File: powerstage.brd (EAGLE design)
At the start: 42 x 43.5 mm, 42 parts, among them CON1 PINHEAD_1X10-2-FEMALE, CON2 BATTERY_CON-2P-XT30-RA, CON3 PINHEAD_1X10-2-FEMALE, IC5 MCP9700, Q1 BUK9K6R2-40E,115, Q2 BUK9K6R2-40E,115, Q3 BUK9K6R2-40E,115

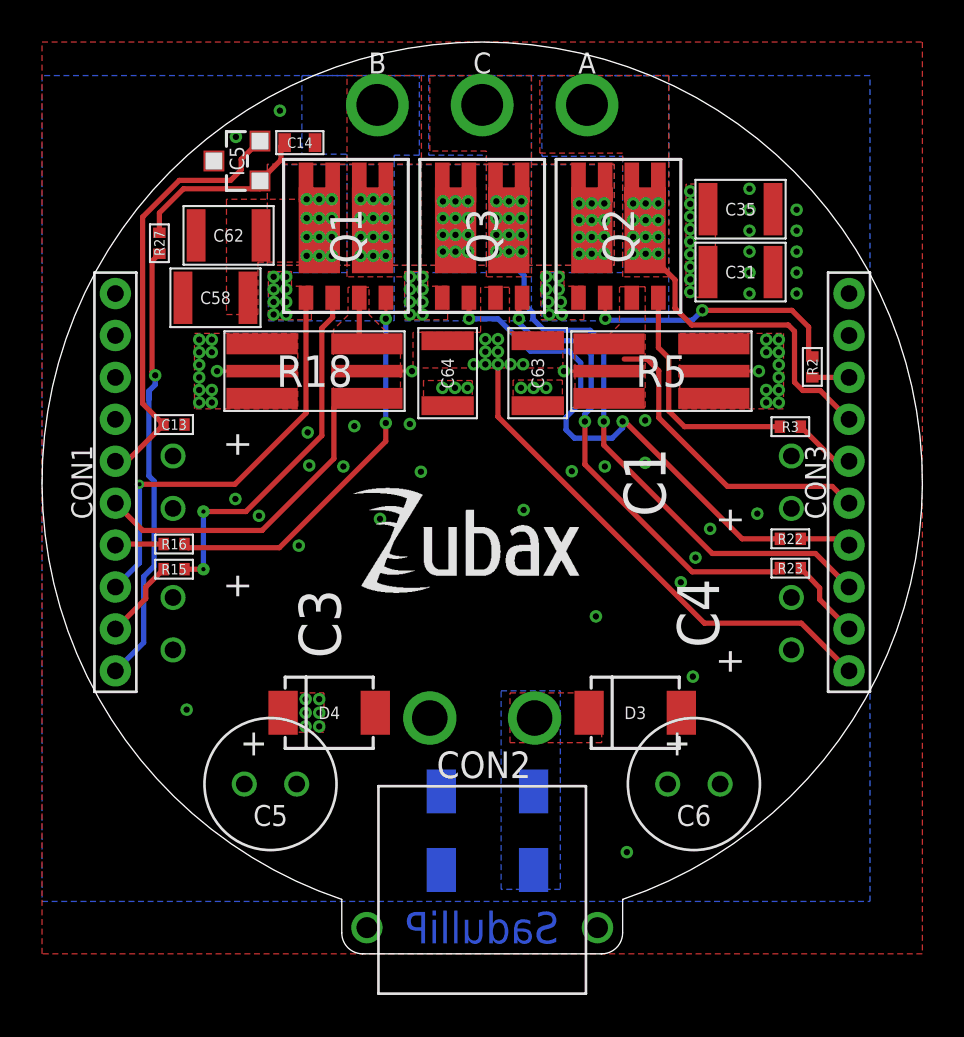
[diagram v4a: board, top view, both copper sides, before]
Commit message: proper powerstage outline
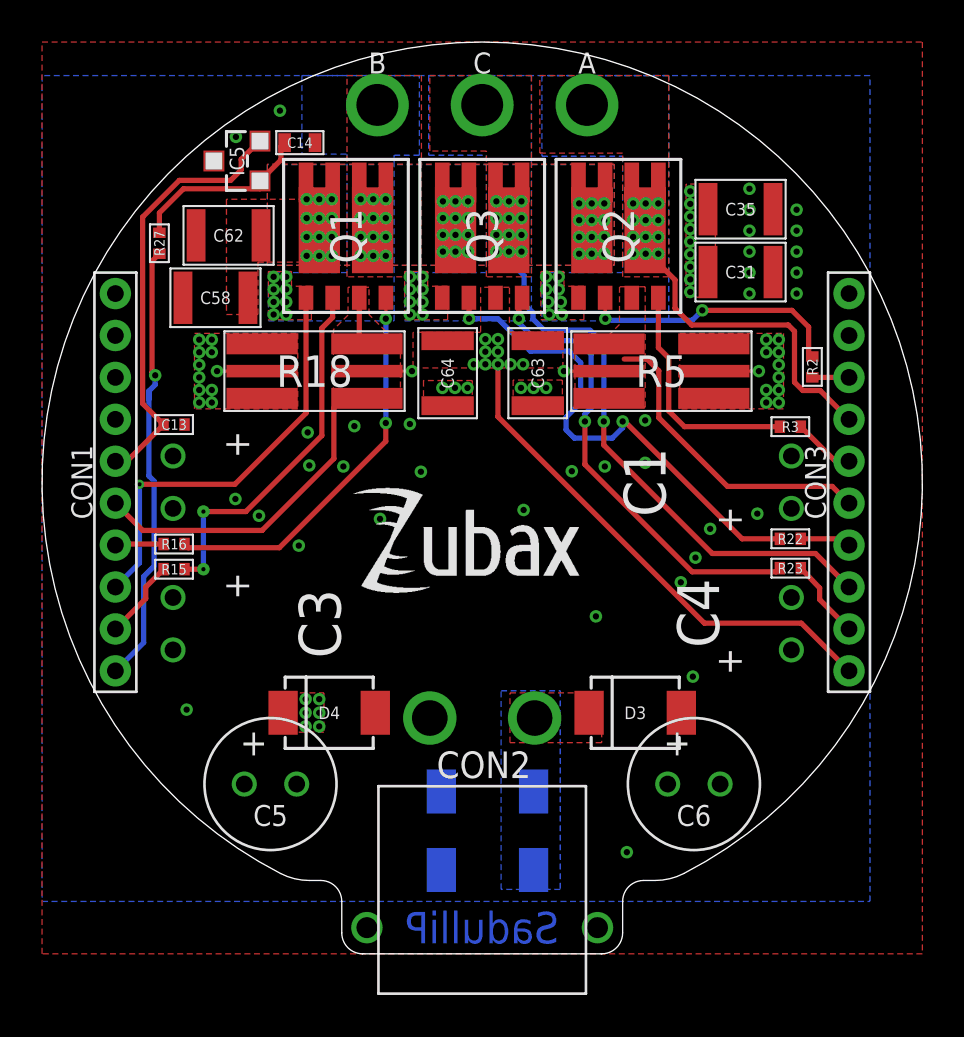
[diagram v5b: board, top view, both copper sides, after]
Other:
- outline, holes or cut-outs redrawn
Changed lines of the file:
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@@
 <drawing>
 <settings>
-<setting alwaysvectorfont="no"/>
+<setting alwaysvectorfont="yes"/>
 <setting verticaltext="up"/>
 </settings>
-<grid distance="0.025" unitdist="mm" unit="mm" style="lines" multiple="2" display="yes" altdistance="5" altunitdist="mil" altunit="mil"/>
+<grid distance="21" unitdist="mm" unit="mm" style="lines" multiple="1" display="yes" altdistance="5" altunitdist="mil" altunit="mil"/>
 <layers>
 <layer number="1" name="Top" color="4" fill="1" visible="yes" active="yes"/>
@@
 <layer number="17" name="Pads" color="2" fill="1" visible="yes" active="yes"/>
 <layer number="18" name="Vias" color="2" fill="1" visible="yes" active="yes"/>
-<layer number="19" name="Unrouted" color="6" fill="1" visible="yes" active="yes"/>
+<layer number="19" name="Unrouted" color="6" fill="1" visible="no" active="yes"/>
 <layer number="20" name="Dimension" color="24" fill="1" visible="yes" active="yes"/>
 <layer number="21" name="tPlace" color="7" fill="1" visible="yes" active="yes"/>
@@
 <layer number="25" name="tNames" color="7" fill="1" visible="yes" active="yes"/>
 <layer number="26" name="bNames" color="7" fill="1" visible="no" active="yes"/>
-<layer number="27" name="tValues" color="7" fill="1" visible="yes" active="yes"/>
+<layer number="27" name="tValues" color="7" fill="1" visible="no" active="yes"/>
 <layer number="28" name="bValues" color="7" fill="1" visible="no" active="yes"/>
 <layer number="29" name="tStop" color="7" fill="3" visible="no" active="yes"/>
@@
 <layer number="39" name="tKeepout" color="4" fill="11" visible="no" active="yes"/>
 <layer number="40" name="bKeepout" color="1" fill="11" visible="no" active="yes"/>
-<layer number="41" name="tRestrict" color="4" fill="10" visible="yes" active="yes"/>
+<layer number="41" name="tRestrict" color="4" fill="10" visible="no" active="yes"/>
 <layer number="42" name="bRestrict" color="1" fill="10" visible="no" active="yes"/>
 <layer number="43" name="vRestrict" color="2" fill="10" visible="no" active="yes"/>
 <layer number="44" name="Drills" color="7" fill="1" visible="no" active="yes"/>
-<layer number="45" name="Holes" color="7" fill="1" visible="yes" active="yes"/>
+<layer number="45" name="Holes" color="7" fill="1" visible="no" active="yes"/>
 <layer number="46" name="Milling" color="3" fill="1" visible="no" active="yes"/>
 <layer number="47" name="Measures" color="7" fill="1" visible="no" active="yes"/>
 <layer number="48" name="Document" color="7" fill="1" visible="no" active="yes"/>
 <layer number="49" name="Reference" color="7" fill="1" visible="no" active="yes"/>
-<layer number="50" name="dxf" color="7" fill="1" visible="yes" active="yes"/>
+<layer number="50" name="dxf" color="7" fill="1" visible="no" active="yes"/>
 <layer number="51" name="tDocu" color="7" fill="1" visible="yes" active="yes"/>
 <layer number="52" name="bDocu" color="7" fill="1" visible="no" active="yes"/>
@@
 <layer number="200" name="200bmp" color="1" fill="10" visible="no" active="yes"/>
 <layer number="201" name="201bmp" color="2" fill="10" visible="no" active="yes"/>
-<layer number="202" name="202bmp" color="3" fill="10" visible="yes" active="yes"/>
+<layer number="202" name="202bmp" color="3" fill="10" visible="no" active="yes"/>
 <layer number="203" name="203bmp" color="4" fill="10" visible="no" active="yes"/>
 <layer number="204" name="204bmp" color="5" fill="10" visible="no" active="yes"/>
@@
 </layers>
 <board>
+<fusionsync huburn="a.cGVyc29uYWw6dWUyYWE4ZDY4" projecturn="a.cGVyc29uYWw6dWUyYWE4ZDY4IzIwMTgxMTA4MTU5MTUwNTA2" f3durn="urn:adsk.wipprod:dm.lineage:WMvf5TlhTr-rsM2oKWPy9g" pcbguid="d1d67abc-637e-4fcf-8898-076f957fbd4c" lastpulledtime="2018-11-11T10:26:16Z" lastsyncedchangeguid="7b521676-cce6-4d0c-938e-80afe84c0ae0"/>
 <plain>
 <wire x1="0" y1="0" x2="0" y2="21" width="0.1524" layer="49" style="shortdash" locked="yes"/>
@@
 <wire x1="20" y1="-20" x2="-20" y2="-20" width="0.01" layer="48" locked="yes"/>
 <wire x1="-20" y1="-20" x2="-20" y2="0" width="0.01" layer="48" locked="yes"/>
-<wire x1="-6.7" y1="-19.9025" x2="-6.7" y2="-21.5" width="0.01" layer="20"/>
-<wire x1="-6.7" y1="-21.5" x2="-5.7" y2="-22.5" width="0.01" layer="20" curve="90"/>
-<wire x1="-5.7" y1="-22.5" x2="5.7" y2="-22.5" width="0.01" layer="20"/>
-<wire x1="5.7" y1="-22.5" x2="6.7" y2="-21.5" width="0.01" layer="20" curve="90"/>
-<wire x1="6.7" y1="-21.5" x2="6.7" y2="-19.9025" width="0.01" layer="20"/>
-<wire x1="6.7" y1="-19.9025" x2="-6.7" y2="-19.9025" width="0.01" layer="20" curve="322.789323"/>
 <wire x1="-0.725" y1="9.45" x2="1.375" y2="9.45" width="0.15" layer="41"/>
 <wire x1="1.375" y1="7.5" x2="1.375" y2="9.45" width="0.15" layer="41"/>
@@
 <wire x1="18.5" y1="10" x2="18.5" y2="-10" width="0.15" layer="41"/>
 <text x="0" y="-22" size="1.5" layer="16" font="vector" ratio="15" rot="MR0" align="bottom-center">SadulliP</text>
+<circle x="0" y="0" radius="21" width="0.1524" layer="49"/>
+<wire x1="7.7" y1="-19" x2="8.2462" y2="-19" width="0.01" layer="20"/>
+<wire x1="8.2462" y1="-19" x2="9.6206" y2="-18.6667" width="0.01" layer="20" curve="27.266025"/>
+<wire x1="9.6206" y1="-18.6667" x2="-9.6206" y2="-18.6667" width="0.01" layer="20" curve="305.467924"/>
+<wire x1="-9.6206" y1="-18.6667" x2="-8.2462" y2="-19" width="0.01" layer="20" curve="27.266037"/>
+<wire x1="-8.2462" y1="-19" x2="-7.7" y2="-19" width="0.01" layer="20"/>
+<wire x1="-7.7" y1="-19" x2="-6.7" y2="-20" width="0.01" layer="20" curve="-89.999995"/>
+<wire x1="-6.7" y1="-20" x2="-6.7" y2="-21.5" width="0.01" layer="20"/>
+<wire x1="-6.7" y1="-21.5" x2="-5.7" y2="-22.5" width="0.01" layer="20" curve="90.000002"/>
+<wire x1="-5.7" y1="-22.5" x2="5.7" y2="-22.5" width="0.01" layer="20"/>
+<wire x1="5.7" y1="-22.5" x2="6.7" y2="-21.5" width="0.01" layer="20" curve="90"/>
+<wire x1="6.7" y1="-21.5" x2="6.7" y2="-20" width="0.01" layer="20"/>
+<wire x1="6.7" y1="-20" x2="7.7" y2="-19" width="0.01" layer="20" curve="-89.999986"/>
 </plain>
 <attributes>
@@
 <wire x1="11.7" y1="-0.2" x2="16.7" y2="-0.2" width="0.25" layer="1"/>
 <wire x1="8.425" y1="3.075" x2="11.7" y2="-0.2" width="0.25" layer="1"/>
-<wire x1="6.775" y1="5.875" x2="6.05" y2="4" width="0" layer="19" extent="1-1"/>
+<wire x1="6.05" y1="4" x2="6.775" y2="5.875" width="0" layer="19" extent="1-1"/>
 </signal>
 <signal name="PHASE_A" class="1">
@@
 </note>
 <note version="8.3" severity="warning">
+Since Version 8.3, EAGLE supports Fusion synchronisation.
+This feature will not be available in this version and saving
+the document will break the link to the Fusion PCB feature.
+</note>
+<note version="8.3" severity="warning">

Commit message: bloody connectors had to be moved
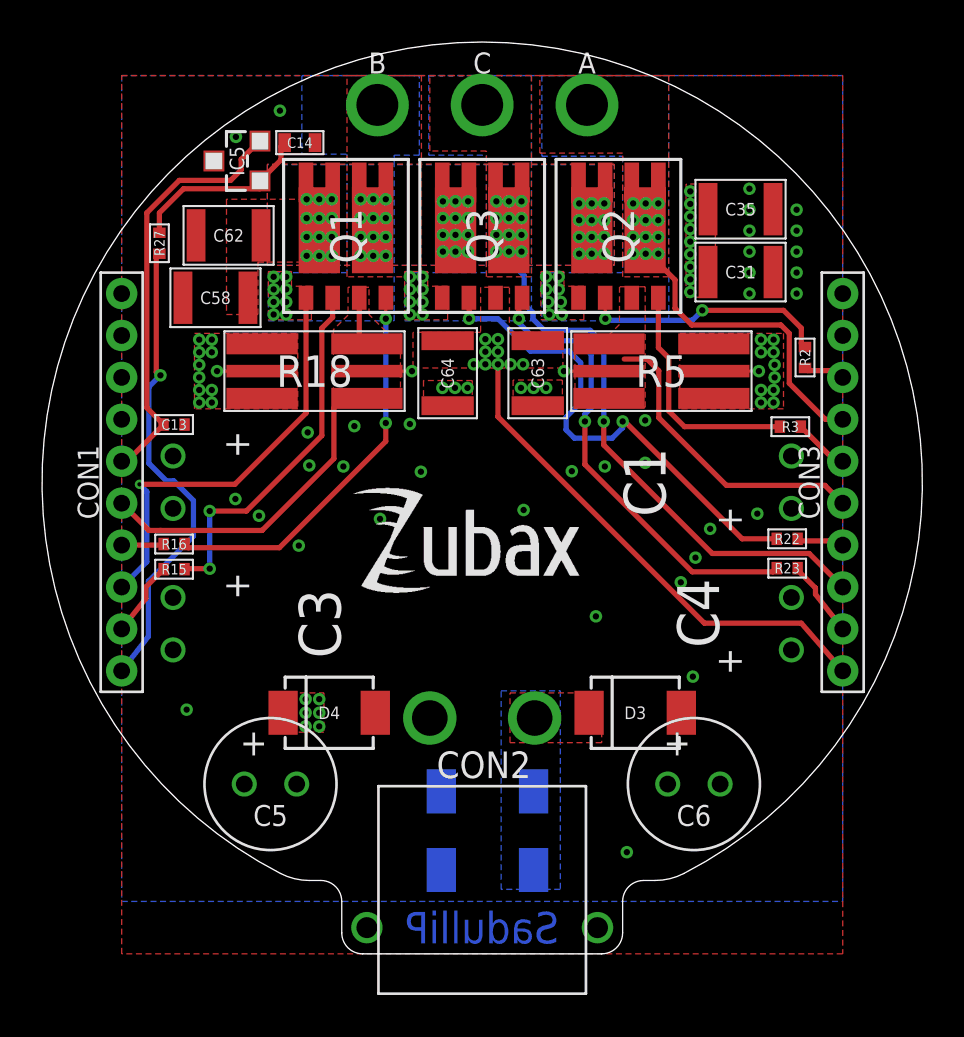
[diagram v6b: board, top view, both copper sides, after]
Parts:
- moved R2 0.57 mm to (15.4, 5.95)
- moved CON1 0.30 mm to (-17.2, 0.00)
- moved CON3 0.30 mm to (17.2, 0.00)
- moved R22 0.15 mm to (14.6, -2.70)
- moved R23 0.15 mm to (14.6, -4.10)
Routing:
- net VDD_5V: track 21.5 -> 22.7 mm
- net N$1: track 12.7 -> 11.9 mm
